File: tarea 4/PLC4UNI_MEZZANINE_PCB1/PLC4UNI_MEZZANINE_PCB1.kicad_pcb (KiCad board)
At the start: 2 copper layers, 37.6 x 39.8 mm, 23 parts, among them J1 PZ254R-12-16P, J2 FPC-05FB-30PH20, U1 MC-121-L119, U2 MT9700-N

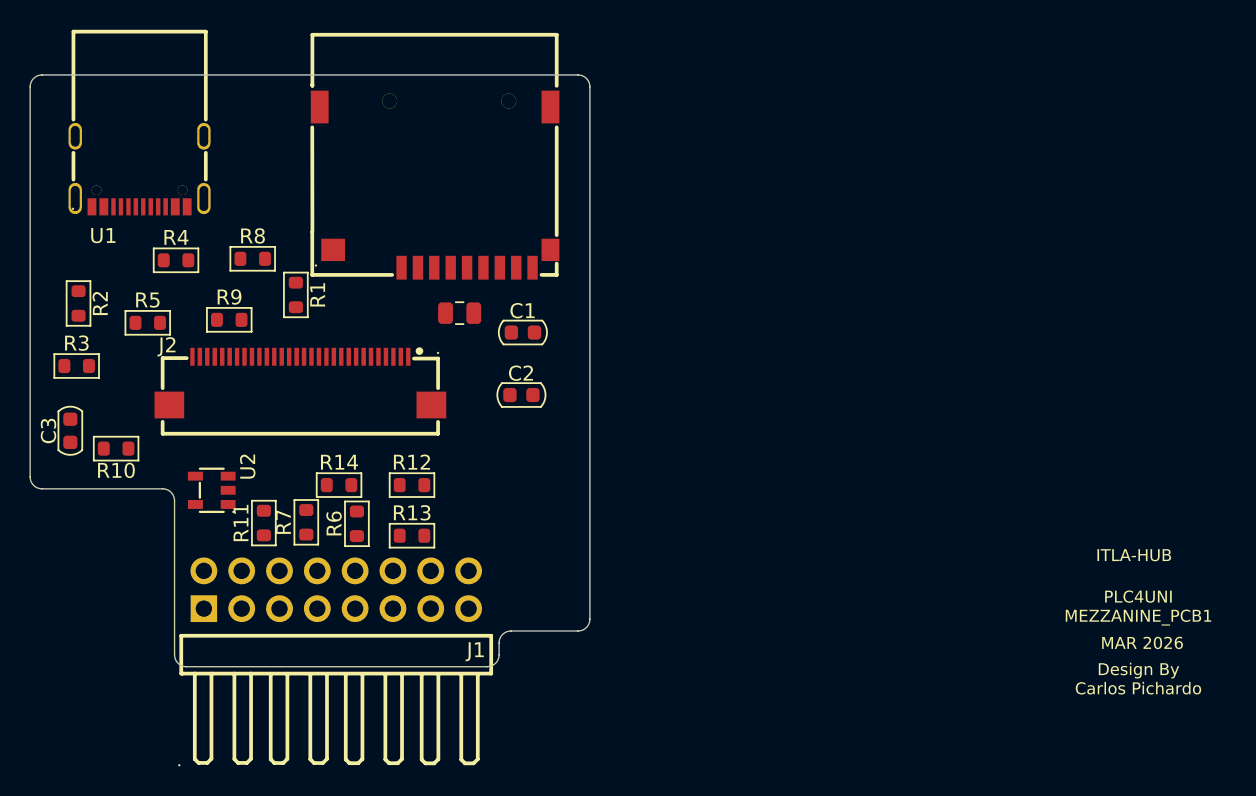
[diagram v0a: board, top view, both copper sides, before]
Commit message: actualizar Mezzanine y Assembly
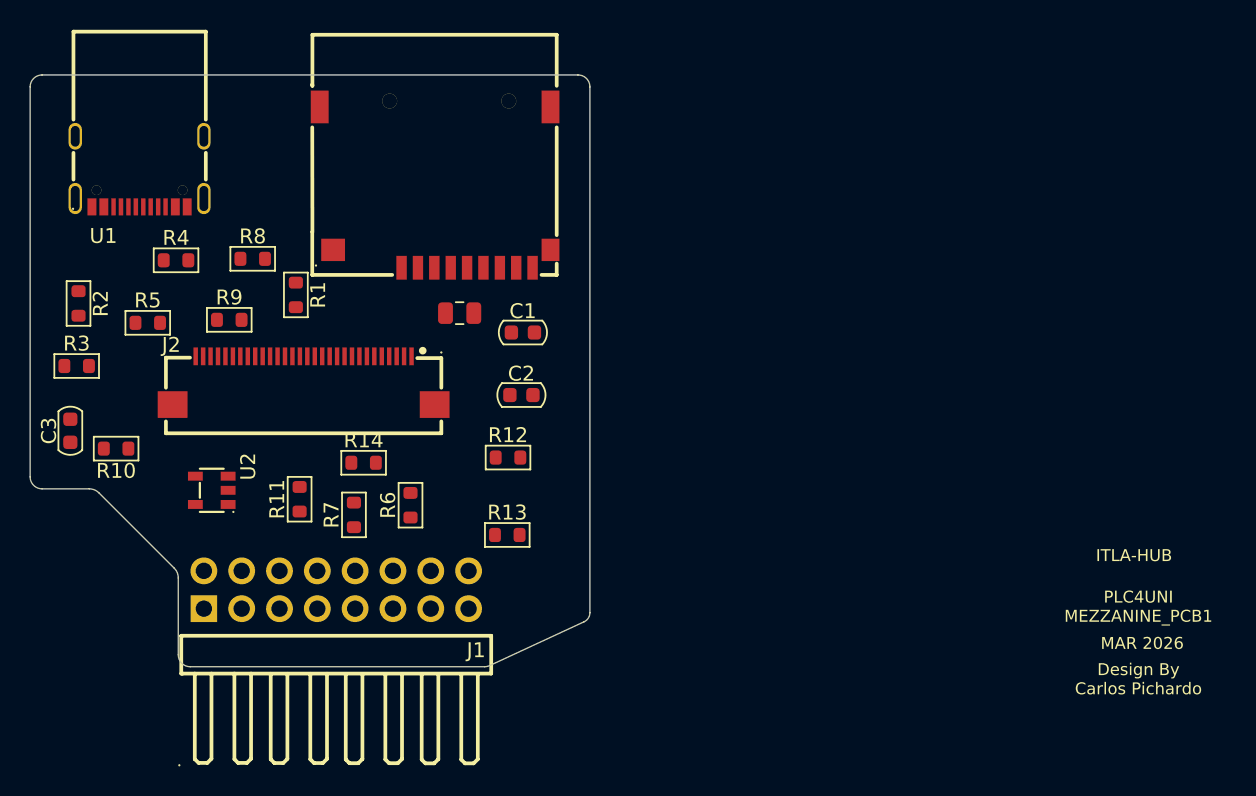
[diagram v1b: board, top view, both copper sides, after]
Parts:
- moved R12 6.71 mm to (122.6, 89.6)
- moved R13 6.40 mm to (122.6, 94.8)
- moved R6 3.81 mm to (116.1, 92.8)
- moved R7 3.24 mm to (112.3, 93.5)
- moved R11 2.88 mm to (108.6, 92.4)
- moved R14 2.23 mm to (112.9, 90.0)
- moved J2 0.22 mm to (108.9, 84.5)
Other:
- outline, holes or cut-outs redrawn
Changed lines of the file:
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@@
 		(allow_soldermask_bridges_in_footprints no)
 		(tenting front back)
-		(aux_axis_origin 90.544 103.682)
-		(grid_origin 98.044 103.632)
+		(grid_origin 90.544 103.682)
 		(pcbplotparams
 			(layerselection 0x00000000_00000000_55555555_5755f5ff)
@@
 	(footprint "Resistor_SMD_AKL:R_0603_1608Metric"
 		(layer "F.Cu")
-		(at 116.194 94.882)
+		(at 122.594 94.832)
 		(descr "Resistor SMD 0603 (1608 Metric), square (rectangular) end terminal, IPC_7351 nominal, (Body size source: IPC-SM-782 page 72, https://www.pcb-3d.com/wordpress/wp-content/uploads/ipc-sm-782a_amendment_1_and_2.pdf), Alternate KiCad Library")
 		(tags "resistor")
@@
 	(footprint "EasyEDA:FPC-SMD_30P-P0.50_FPC-05FB-30PH20"
 		(layer "F.Cu")
-		(at 108.694 84.482)
+		(at 108.914 84.452)
 		(property "Reference" "J2"
 			(at -8.89 -2.382 0)
@@
 	(footprint "Resistor_SMD_AKL:R_0603_1608Metric"
 		(layer "F.Cu")
-		(at 116.194 91.482)
+		(at 122.644 89.632)
 		(descr "Resistor SMD 0603 (1608 Metric), square (rectangular) end terminal, IPC_7351 nominal, (Body size source: IPC-SM-782 page 72, https://www.pcb-3d.com/wordpress/wp-content/uploads/ipc-sm-782a_amendment_1_and_2.pdf), Alternate KiCad Library")
 		(tags "resistor")
@@
 	(footprint "Resistor_SMD_AKL:R_0603_1608Metric"
 		(layer "F.Cu")
-		(at 112.494 94.082 90)
+		(at 116.094 92.832 90)
 		(descr "Resistor SMD 0603 (1608 Metric), square (rectangular) end terminal, IPC_7351 nominal, (Body size source: IPC-SM-782 page 72, https://www.pcb-3d.com/wordpress/wp-content/uploads/ipc-sm-782a_amendment_1_and_2.pdf), Alternate KiCad Library")
 		(tags "resistor")
@@
 	(footprint "Resistor_SMD_AKL:R_0603_1608Metric"
 		(layer "F.Cu")
-		(at 106.244 94.032 90)
+		(at 108.644 92.432 90)
 		(descr "Resistor SMD 0603 (1608 Metric), square (rectangular) end terminal, IPC_7351 nominal, (Body size source: IPC-SM-782 page 72, https://www.pcb-3d.com/wordpress/wp-content/uploads/ipc-sm-782a_amendment_1_and_2.pdf), Alternate KiCad Library")
 		(tags "resistor")
@@
 	(footprint "Resistor_SMD_AKL:R_0603_1608Metric"
 		(layer "F.Cu")
-		(at 111.294 91.482)
+		(at 112.944 89.982)
 		(descr "Resistor SMD 0603 (1608 Metric), square (rectangular) end terminal, IPC_7351 nominal, (Body size source: IPC-SM-782 page 72, https://www.pcb-3d.com/wordpress/wp-content/uploads/ipc-sm-782a_amendment_1_and_2.pdf), Alternate KiCad Library")
 		(tags "resistor")
@@
 	(footprint "Resistor_SMD_AKL:R_0603_1608Metric"
 		(layer "F.Cu")
-		(at 109.094 93.982 90)
+		(at 112.294 93.482 90)
 		(descr "Resistor SMD 0603 (1608 Metric), square (rectangular) end terminal, IPC_7351 nominal, (Body size source: IPC-SM-782 page 72, https://www.pcb-3d.com/wordpress/wp-content/uploads/ipc-sm-782a_amendment_1_and_2.pdf), Alternate KiCad Library")
 		(tags "resistor")
@@
 	)
 	(gr_arc
-		(start 101.044 103.682)
-		(mid 100.478315 103.447685)
-		(end 100.244 102.882)
+		(start 101.294 103.682)
+		(mid 100.728315 103.447685)
+		(end 100.494 102.882)
 		(stroke
 			(width 0.05)
 			(type default)
 		)
+		(locked yes)
 		(layer "Edge.Cuts")
 	)
 	(gr_line
-		(start 128.144 100.482)
-		(end 128.144 64.732)
+		(start 121.071664 103.681984)
+		(end 101.294 103.682)
 		(stroke
 			(width 0.05)
 			(type default)
 		)
+		(locked yes)
+		(layer "Edge.Cuts")
+	)
+	(gr_arc
+		(start 121.42241 103.598835)
+		(mid 121.251899 103.660924)
+		(end 121.071664 103.682)
+		(stroke
+			(width 0.05)
+			(type default)
+		)
+		(locked yes)
 		(layer "Edge.Cuts")
 	)
@@
 			(type default)
 		)
+		(locked yes)
 		(layer "Edge.Cuts")
 	)
@@
 			(type default)
 		)
+		(locked yes)
 		(layer "Edge.Cuts")
 	)
 	(gr_line
-		(start 122.844 101.282)
-		(end 127.344 101.282)
+		(start 100.208958 97.047267)
+		(end 95.173932 92.012066)
 		(stroke
 			(width 0.05)
 			(type default)
 		)
+		(locked yes)
 		(layer "Edge.Cuts")
 	)
 	(gr_line
-		(start 122.044 102.882)
-		(end 122.044 102.082)
-		(stroke
-			(width 0.05)
-			(type default)
-		)
-		(layer "Edge.Cuts")
-	)
-	(gr_arc
-		(start 122.044 102.882)
-		(mid 121.809685 103.447685)
-		(end 121.244 103.682)
-		(stroke
-			(width 0.05)
-			(type default)
-		)
-		(layer "Edge.Cuts")
-	)
-	(gr_arc
-		(start 122.044 102.082)
-		(mid 122.278315 101.516315)
-		(end 122.844 101.282)
+		(start 100.494 102.882)
+		(end 100.494 97.714811)
 		(stroke
 			(width 0.05)
 			(type default)
 		)
+		(locked yes)
 		(layer "Edge.Cuts")
 	)
@@
 			(type default)
 		)
+		(locked yes)
 		(layer "Edge.Cuts")
 	)
@@
 			(type default)
 		)
+		(locked yes)
 		(layer "Edge.Cuts")
 	)
 	(gr_line
-		(start 101.044 103.682)
-		(end 121.244 103.682)
+		(start 121.42241 103.598834)
+		(end 127.75069 100.664464)
 		(stroke
 			(width 0.05)
 			(type default)
 		)
+		(locked yes)
 		(layer "Edge.Cuts")
 	)
 	(gr_arc
-		(start 128.144 100.482)
-		(mid 127.909685 101.047685)
-		(end 127.344 101.282)
+		(start 100.208958 97.047266)
+		(mid 100.419758 97.351883)
+		(end 100.494 97.714811)
 		(stroke
 			(width 0.05)
 			(type default)
 		)
+		(locked yes)
 		(layer "Edge.Cuts")
 	)
-	(gr_line
-		(start 100.244 92.532)
-		(end 100.244 102.882)
+	(gr_arc
+		(start 128.144 100.051457)
+		(mid 128.037175 100.415663)
+		(end 127.750548 100.664464)
 		(stroke
 			(width 0.05)
 			(type default)
 		)
+		(locked yes)
 		(layer "Edge.Cuts")
 	)
 	(gr_arc
-		(start 99.444 91.732)
-		(mid 100.009685 91.966315)
-		(end 100.244 92.532)
+		(start 94.511317 91.732)
+		(mid 94.871003 91.804892)
+		(end 95.173932 92.012066)
 		(stroke
 			(width 0.05)
 			(type default)
 		)
+		(locked yes)
 		(layer "Edge.Cuts")
 	)
 	(gr_line
-		(start 91.344 91.732)
-		(end 99.444 91.732)
+		(start 128.144 100.0515)
+		(end 128.144 64.732)
 		(stroke
 			(width 0.05)
 			(type default)
 		)
+		(locked yes)
 		(layer "Edge.Cuts")
 	)
@@
 			(type default)
 		)
+		(locked yes)
+		(layer "Edge.Cuts")
+	)
+	(gr_line
+		(start 94.511317 91.732)
+		(end 91.344 91.732)
+		(stroke
+			(width 0.05)
+			(type default)
+		)
+		(locked yes)
 		(layer "Edge.Cuts")
 	)
@@
 	)
 	(group ""
-		(members "24560c61-5cea-47a1-b3c4-16a09b391786" "24701ce3-768f-420e-b695-19041dbf3307"
-			"40355e4f-1247-44aa-99aa-451eaf3d77ec" "5acec4d6-f9e2-4607-a91d-0ee8fa758f68"
-			"6547a1d5-6fa4-44a8-a207-13fc270cff59" "81883187-aea4-4256-adc4-4e7aedc93e75"
-			"834c79be-627a-4b2a-825c-5475e8493b4f" "8ed91bcc-63c8-4013-9081-1d0fa9ec3686"
-			"90cb0f35-8fcd-4bfd-b5a3-79b848921d5f" "9a13abc3-d069-457c-b1b0-7111c789bec6"
-			"c0ae9445-9b78-4343-a3c9-cd4cf37eef41" "c85a8c41-fa0c-48cf-9a6a-f92781147d5e"
-			"e73c7374-e3a0-4c0c-b9e5-8b1be1680352" "ed233680-0c50-45e9-b8b7-07b411c14193"
-			"f183d82b-e083-42de-a239-3ef9b2eca8c6" "f3c607e4-a553-49d9-88f2-f40f4ac73ca5"
+		(locked yes)
+		(members "1397b72e-0e9d-4178-a2fb-9a94c792954d" "21ffb474-74c4-4001-8228-0e1df44649d9"
+			"29ba6765-58da-4a99-945a-412cbc285bcb" "40355e4f-1247-44aa-99aa-451eaf3d77ec"
+			"5acec4d6-f9e2-4607-a91d-0ee8fa758f68" "60e8a81c-0f2f-4dbb-a00a-ff2f5ad7707a"
+			"87a68999-09ac-4956-9b55-0ce6a26ea860" "90cb0f35-8fcd-4bfd-b5a3-79b848921d5f"
+			"9a13abc3-d069-457c-b1b0-7111c789bec6" "b357368e-7abf-4f3d-a1c1-a9ad32664c02"
+			"c8591aee-dff3-42fc-8151-447497acb44e" "cd49e28c-4e8b-41bc-9125-6d33ff28cd40"
+			"d3dfdb71-ddd7-4124-979c-a5127e6b18b9" "eb064ab6-6a03-4382-bd66-5e2294376eed"
+			"f3c607e4-a553-49d9-88f2-f40f4ac73ca5" "fbc22410-e401-4447-9a7e-e82dcdb26856"
 		)
 	)
